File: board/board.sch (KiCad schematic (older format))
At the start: 20 parts, among them CON1 NRF24L01+MODULE, CON2 AVR-ISP-6, IC1 ATMEGA88PA-A, SW1 SW_PUSH, U1 XR1151

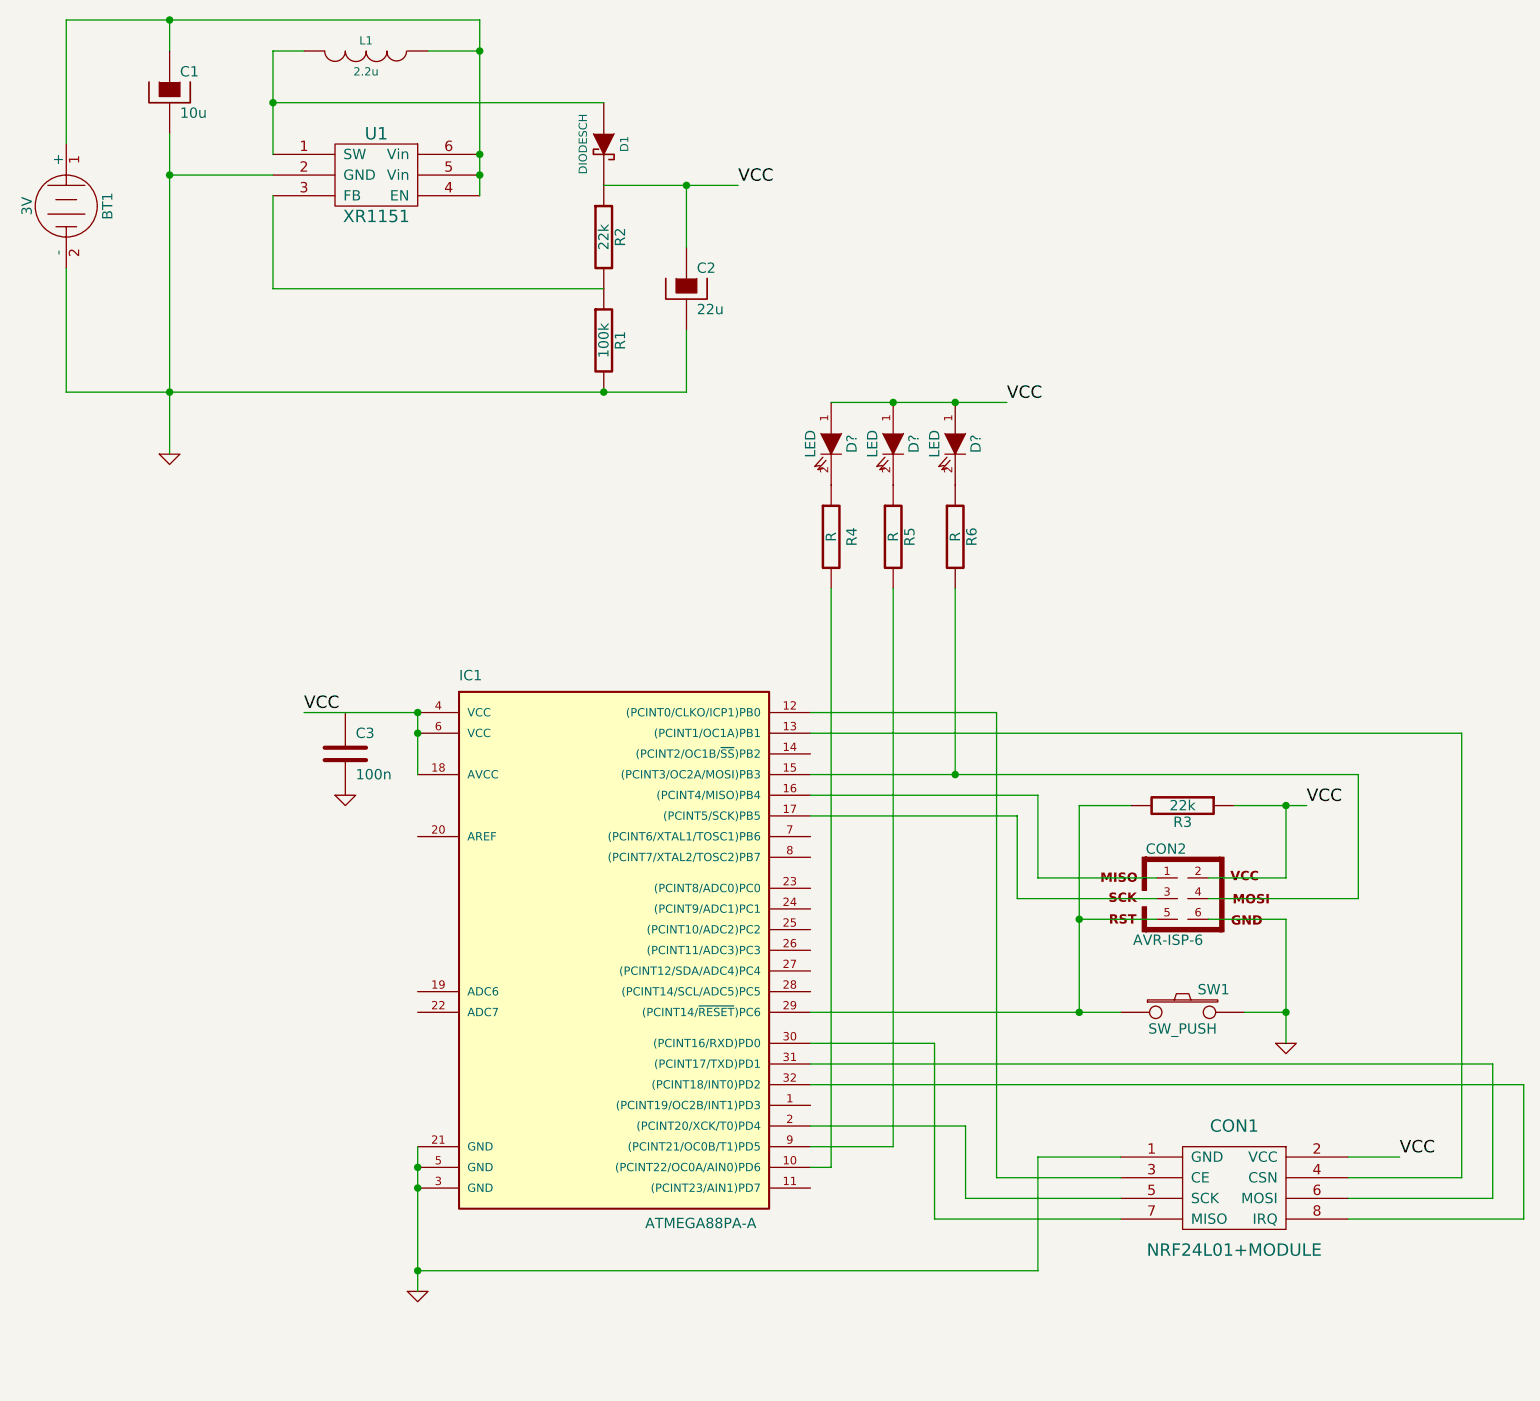
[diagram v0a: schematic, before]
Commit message: - Moved CSN to a less useful pin  - Added points to connect the LEDs to OC1, for the ATmega8
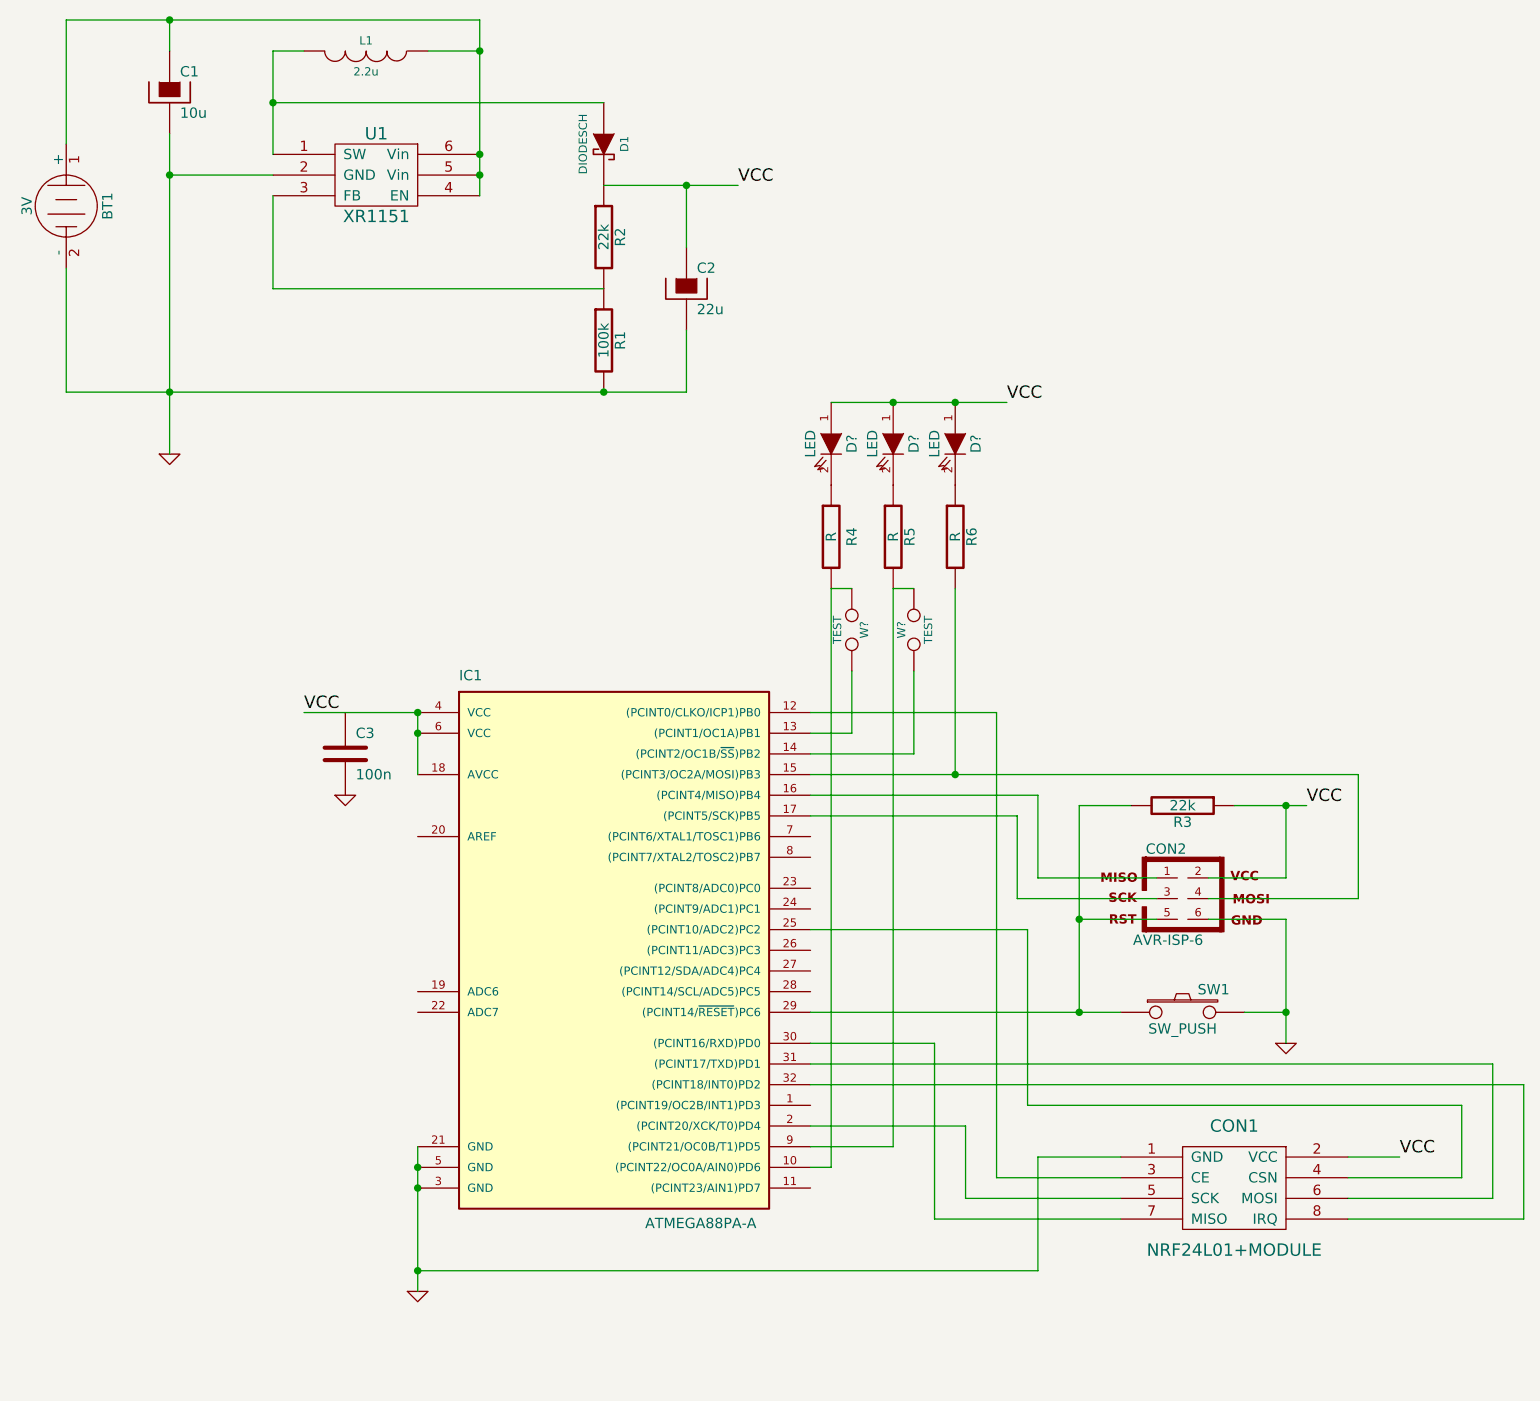
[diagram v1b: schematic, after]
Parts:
- added W? (x2): TEST, symbol TEST
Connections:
- net at CON1.4 (CSN): now also IC1.25 ((PCINT10/ADC2)PC2); no longer IC1.13 ((PCINT1/OC1A)PB1)
- net at IC1.10 ((PCINT22/OC0A/AIN0)PD6), R4.2: now also W?.1
- net at IC1.14 ((PCINT2/OC1B/~SS~)PB2): now also W?.1
- net at IC1.9 ((PCINT21/OC0B/T1)PD5), R5.2: now also W?.2
- new net: IC1.13 ((PCINT1/OC1A)PB1), W?.2
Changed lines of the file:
@@
-EESchema Schematic File Version 2  date Sun 23 Mar 2014 19:38:26 CST
+EESchema Schematic File Version 2  date Tue 25 Mar 2014 21:10:04 CST
 LIBS:power
 LIBS:device
@@
 Sheet 1 1
 Title ""
-Date "23 mar 2014"
+Date "25 mar 2014"
 Rev ""
 Comp ""
@@
 $EndDescr
 Wire Wire Line
-	7200 6700 7750 6700
-Wire Wire Line
-	1000 1100 1500 1100
-Wire Wire Line
-	1500 1100 3000 1100
-Wire Wire Line
-	1000 2900 1500 2900
-Wire Wire Line
-	1500 2900 3600 2900
-Wire Wire Line
-	3600 2900 4000 2900
-Wire Wire Line
-	1000 2900 1000 2300
+	4600 4650 5100 4650
+Wire Wire Line
+	5100 4650 5100 4250
+Wire Wire Line
+	5100 3850 5000 3850
+Wire Wire Line
+	4800 4250 4800 4550
+Wire Wire Line
+	4800 4550 4600 4550
+Wire Wire Line
+	4600 5500 5650 5500
+Wire Wire Line
+	5650 5500 5650 6350
+Wire Wire Line
+	5650 6350 7750 6350
+Wire Wire Line
+	7750 6350 7750 6700
+Connection ~ 2700 4550
+Wire Wire Line
+	2700 4750 2700 4450
+Wire Wire Line
+	3000 1950 3000 1100
+Connection ~ 1500 1100
+Wire Wire Line
+	1000 1700 1000 1100
+Connection ~ 6900 5900
+Wire Wire Line
+	6700 5900 6900 5900
+Connection ~ 6900 4900
+Wire Wire Line
+	6650 4900 7000 4900
+Connection ~ 5900 5450
+Wire Wire Line
+	6275 5450 5900 5450
+Wire Wire Line
+	6150 4900 5900 4900
+Wire Wire Line
+	6275 5350 5600 5350
+Wire Wire Line
+	5600 5350 5600 4950
+Wire Wire Line
+	5600 4950 4600 4950
+Wire Wire Line
+	6525 5250 6900 5250
+Wire Wire Line
+	4600 4850 5700 4850
+Wire Wire Line
+	5700 4850 5700 5250
+Wire Wire Line
+	7200 6800 7900 6800
+Wire Wire Line
+	7900 6800 7900 6150
+Wire Wire Line
+	7900 6150 4600 6150
+Wire Wire Line
+	7200 6600 7450 6600
+Connection ~ 5000 2950
+Wire Wire Line
+	5300 3850 5300 4750
+Wire Wire Line
+	4700 6650 4700 3850
+Wire Wire Line
+	4700 6650 4600 6650
+Wire Wire Line
+	4600 6450 5350 6450
+Wire Wire Line
+	5350 6450 5350 6800
+Wire Wire Line
+	5350 6800 6100 6800
+Connection ~ 2700 6750
+Connection ~ 4000 1900
+Wire Wire Line
+	4250 1900 3600 1900
+Wire Wire Line
+	2700 4450 2150 4450
+Wire Wire Line
+	4000 2200 4000 1900
+Connection ~ 1500 1850
+Wire Wire Line
+	1500 1650 1500 3200
+Connection ~ 2000 1500
+Wire Wire Line
+	3600 1500 2000 1500
+Wire Wire Line
+	3000 1250 2750 1250
+Connection ~ 3000 1250
+Wire Wire Line
+	2000 1850 1500 1850
+Connection ~ 3000 1850
+Connection ~ 3000 1750
+Wire Wire Line
+	3600 2400 2000 2400
+Wire Wire Line
+	2000 2400 2000 1950
+Wire Wire Line
+	2150 1250 2000 1250
+Wire Wire Line
+	2000 1250 2000 1750
+Wire Wire Line
+	1500 1250 1500 1100
+Connection ~ 1500 2900
+Wire Wire Line
+	4000 2600 4000 2900
+Connection ~ 3600 2900
+Wire Wire Line
+	2700 6550 2700 7250
+Connection ~ 2700 6650
+Connection ~ 2700 4450
+Wire Wire Line
+	6100 6900 5200 6900
+Wire Wire Line
+	5200 6900 5200 6050
+Wire Wire Line
+	5200 6050 4600 6050
+Wire Wire Line
+	6100 6700 5500 6700
+Wire Wire Line
+	5500 6700 5500 4450
+Wire Wire Line
+	5500 4450 4600 4450
+Wire Wire Line
+	2700 7150 5700 7150
+Connection ~ 2700 7150
+Wire Wire Line
+	5700 7150 5700 6600
+Wire Wire Line
+	5700 6600 6100 6600
+Wire Wire Line
+	4600 6550 5000 6550
+Wire Wire Line
+	5000 6550 5000 3850
+Wire Wire Line
+	5550 2950 4700 2950
+Connection ~ 5300 2950
+Wire Wire Line
+	4600 6250 8050 6250
+Wire Wire Line
+	8050 6250 8050 6900
+Wire Wire Line
+	8050 6900 7200 6900
+Wire Wire Line
+	4600 4750 7250 4750
+Connection ~ 5300 4750
+Wire Wire Line
+	5700 5250 6275 5250
+Wire Wire Line
+	6900 5250 6900 4900
+Wire Wire Line
+	5900 4900 5900 5900
+Wire Wire Line
+	6525 5450 6900 5450
+Wire Wire Line
+	6900 5450 6900 6050
+Wire Wire Line
+	7250 4750 7250 5350
+Wire Wire Line
+	7250 5350 6525 5350
+Wire Wire Line
+	4600 5900 6100 5900
 Connection ~ 5900 5900
 Wire Wire Line
-	6100 5900 5900 5900
-Wire Wire Line
-	5900 5900 4600 5900
-Wire Wire Line
-	6525 5350 7250 5350
-Wire Wire Line
-	7250 5350 7250 4750
-Wire Wire Line
-	6900 6050 6900 5900
-Wire Wire Line
-	6900 5900 6900 5450
-Wire Wire Line
-	6900 5450 6525 5450
-Wire Wire Line
-	5900 5900 5900 5450
-Wire Wire Line
-	5900 5450 5900 4900
-Wire Wire Line
-	6900 4900 6900 5250
-Wire Wire Line
-	6275 5250 5700 5250
-Connection ~ 5300 4750
-Wire Wire Line
-	7250 4750 5300 4750
-Wire Wire Line
-	5300 4750 4600 4750
-Wire Wire Line
-	7750 6700 7750 4550
-Wire Wire Line
-	7750 4550 4600 4550
-Wire Wire Line
-	7200 6900 8050 6900
-Wire Wire Line
-	8050 6900 8050 6250
-Wire Wire Line
-	8050 6250 4600 6250
-Connection ~ 5300 2950
-Wire Wire Line
-	4700 2950 5000 2950
-Wire Wire Line
-	5000 2950 5300 2950
-Wire Wire Line
-	5300 2950 5550 2950
-Wire Wire Line
-	5000 3850 5000 6550
-Wire Wire Line
-	5000 6550 4600 6550
-Wire Wire Line
-	6100 6600 5700 6600
-Wire Wire Line
-	5700 6600 5700 7150
-Connection ~ 2700 7150
-Wire Wire Line
-	5700 7150 2700 7150
-Wire Wire Line
-	4600 4450 5500 4450
-Wire Wire Line
-	5500 4450 5500 6700
-Wire Wire Line
-	5500 6700 6100 6700
-Wire Wire Line
-	4600 6050 5200 6050
-Wire Wire Line
-	5200 6050 5200 6900
-Wire Wire Line
-	5200 6900 6100 6900
-Connection ~ 2700 4450
-Connection ~ 2700 6650
-Wire Wire Line
-	2700 7250 2700 7150
-Wire Wire Line
-	2700 7150 2700 6750
-Wire Wire Line
-	2700 6750 2700 6650
-Wire Wire Line
-	2700 6650 2700 6550
-Connection ~ 3600 2900
-Wire Wire Line
-	4000 2900 4000 2600
-Connection ~ 1500 2900
-Wire Wire Line
-	1500 1100 1500 1250
-Wire Wire Line
-	2000 1750 2000 1500
-Wire Wire Line
-	2000 1500 2000 1250
-Wire Wire Line
-	2000 1250 2150 1250
-Wire Wire Line
-	2000 1950 2000 2400
-Wire Wire Line
-	2000 2400 3600 2400
-Connection ~ 3000 1750
-Connection ~ 3000 1850
-Wire Wire Line
-	2000 1850 1500 1850
-Connection ~ 3000 1250
-Wire Wire Line
-	3000 1250 2750 1250
-Wire Wire Line
-	3600 1500 2000 1500
-Connection ~ 2000 1500
-Wire Wire Line
-	1500 3200 1500 2900
-Wire Wire Line
-	1500 2900 1500 1850
-Wire Wire Line
-	1500 1850 1500 1650
-Connection ~ 1500 1850
-Wire Wire Line
-	4000 2200 4000 1900
-Wire Wire Line
-	2150 4450 2700 4450
-Wire Wire Line
-	3600 1900 4000 1900
-Wire Wire Line
-	4000 1900 4250 1900
-Connection ~ 4000 1900
-Connection ~ 2700 6750
-Wire Wire Line
-	6100 6800 5350 6800
-Wire Wire Line
-	5350 6800 5350 6450
-Wire Wire Line
-	5350 6450 4600 6450
-Wire Wire Line
-	4600 6650 4700 6650
-Wire Wire Line
-	4700 6650 4700 3850
-Wire Wire Line
-	5300 3850 5300 4750
-Connection ~ 5000 2950
-Wire Wire Line
-	7200 6600 7450 6600
-Wire Wire Line
-	4600 6150 7900 6150
-Wire Wire Line
-	7900 6150 7900 6800
-Wire Wire Line
-	7900 6800 7200 6800
-Wire Wire Line
-	5700 5250 5700 4850
-Wire Wire Line
-	5700 4850 4600 4850
-Wire Wire Line
-	6900 5250 6525 5250
-Wire Wire Line
-	4600 4950 5600 4950
-Wire Wire Line
-	5600 4950 5600 5350
-Wire Wire Line
-	5600 5350 6275 5350
-Wire Wire Line
-	5900 4900 6150 4900
-Wire Wire Line
-	6275 5450 5900 5450
-Connection ~ 5900 5450
-Wire Wire Line
-	7000 4900 6900 4900
-Wire Wire Line
-	6900 4900 6650 4900
-Connection ~ 6900 4900
-Wire Wire Line
-	6700 5900 6900 5900
-Connection ~ 6900 5900
-Wire Wire Line
-	1000 1100 1000 1700
-Connection ~ 1500 1100
-Wire Wire Line
-	3000 1100 3000 1250
-Wire Wire Line
-	3000 1250 3000 1750
-Wire Wire Line
-	3000 1750 3000 1850
-Wire Wire Line
-	3000 1850 3000 1950
-Wire Wire Line
-	2700 4450 2700 4550
-Wire Wire Line
-	2700 4550 2700 4750
-Connection ~ 2700 4550
+	1000 2300 1000 2900
+Wire Wire Line
+	1000 2900 4000 2900
+Wire Wire Line
+	1000 1100 3000 1100
+Wire Wire Line
+	7750 6700 7200 6700
+Wire Wire Line
+	4700 3850 4800 3850
+$Comp
+L TEST W?
+U 1 1 53315CD1
+P 5100 4050
+F 0 "W?" H 5100 4110 40  0000 C CNN
+F 1 "TEST" H 5100 3980 40  0000 C CNN
+	1    5100 4050
+	0    -1   -1   0
+$EndComp
+$Comp
+L TEST W?
+U 1 1 53315C8D
+P 4800 4050
+F 0 "W?" H 4800 4110 40  0000 C CNN
+F 1 "TEST" H 4800 3980 40  0000 C CNN
+	1    4800 4050
+	0    1    1    0
+$EndComp
 $Comp
 L BATTERY BT1
